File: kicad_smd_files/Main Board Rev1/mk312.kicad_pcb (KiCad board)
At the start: 4 copper layers, 135 x 83.5 mm, 171 parts, among them IC1 LD1086BDTTR, IC2 L7805CV, IC3 L7809ABV, IC4 L7809ABV, J1 Barrel_Jack_MountingPin, J10 OUTPUT B, J11 Conn_01x24_Male, J12 Conn_01x24_Male, J2 +12V Battery, J3 Conn_02x03_Odd_Even, J4 RADIO INTERFACE, J5 MIC INPUT, J6 LINE INPUT, J7 REMOTE INPUT, J8 LINK INPUT, J9 OUTPUT A, Q1 MMBT3904-7-F, Q2 MMBT3904-7-F, Q3 DMN10H170SK3-13, Q4 DMP6180SK3-13, Q5 DMN10H170SK3-13, Q6 DMN10H170SK3-13, Q7 DMP6180SK3-13, Q8 DMN10H170SK3-13, SW2 LEFT/DOWN, SW3 OK, SW4 RIGHT/UP, SW5 MENU, U1 ATmega16-16AU, U2 MCP6L01U, U3 CD4006B, U4 SP232E, U6 LM324N, U7 LM358N, U8 LTC1661

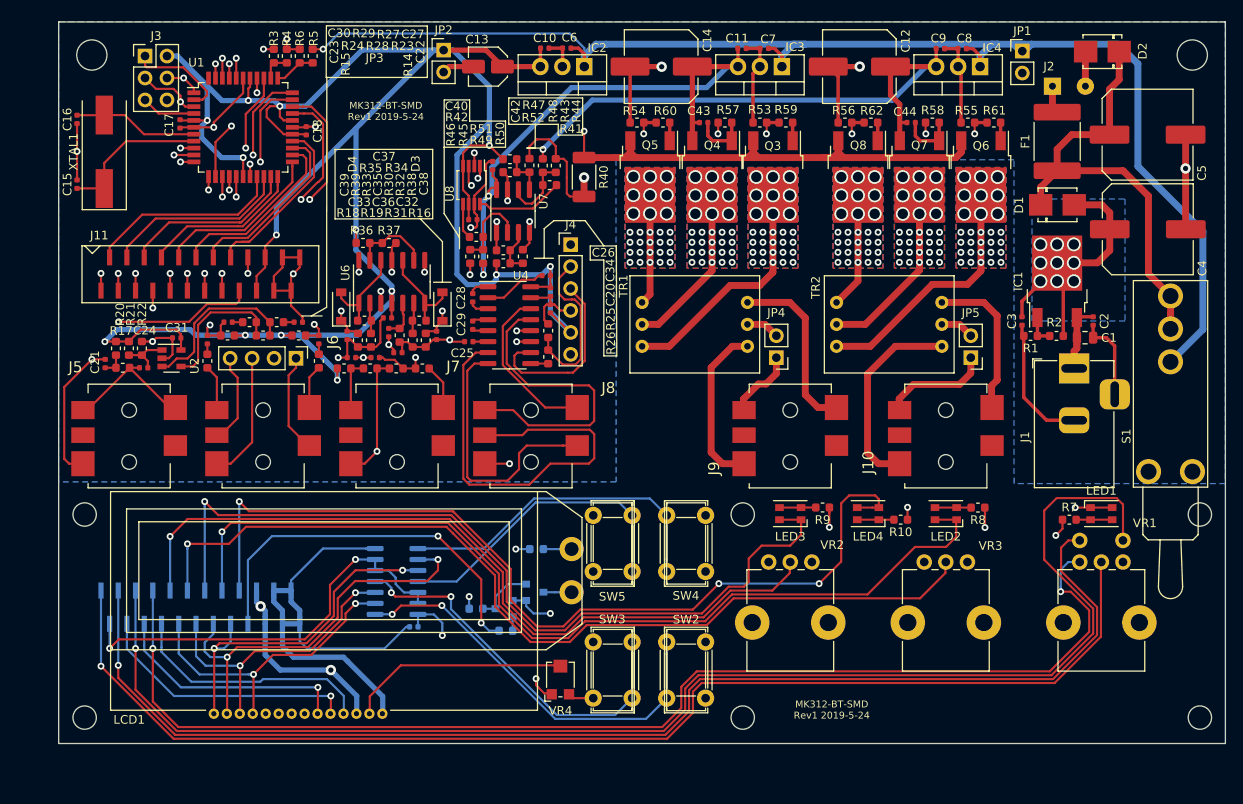
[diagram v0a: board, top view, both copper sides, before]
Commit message: Smaller PCB, cheaper parts
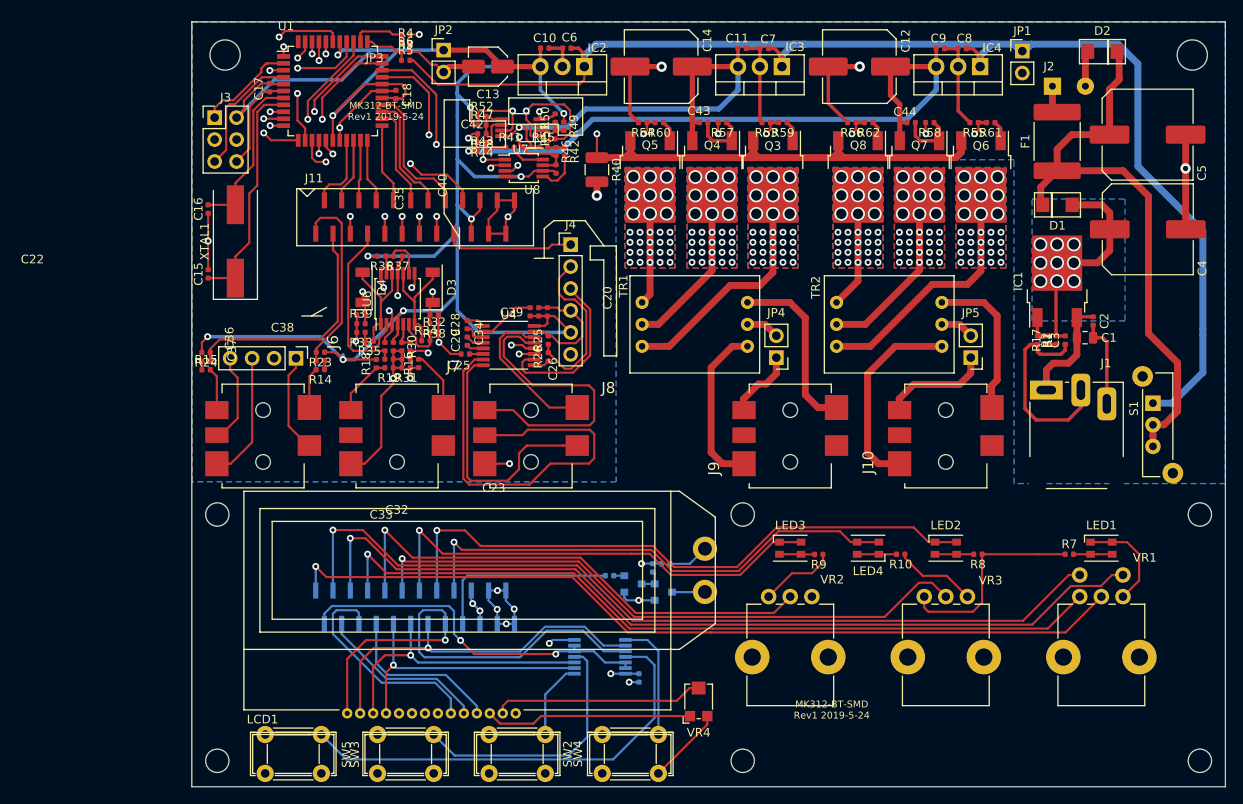
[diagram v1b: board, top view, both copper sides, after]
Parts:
- removed C21, C27, C30: 1uF, Capacitor_SMD:C_0402_1005Metric
- removed C24, C31: 0.1uF, Capacitor_SMD:C_0402_1005Metric
- removed J5: MIC INPUT, mk312-smd-footprints:SJ13515SMTTR
- removed R20: 2.2K, Resistor_SMD:R_0603_1608Metric
- removed R21, R22: 100K, Resistor_SMD:R_0603_1608Metric
- removed R27: 20K, Resistor_SMD:R_0603_1608Metric
- removed R28: 1M, Resistor_SMD:R_0603_1608Metric
- removed R29: 4.7K, Resistor_SMD:R_0603_1608Metric
- removed U2: MCP6L01U, Package_TO_SOT_SMD:SOT-23-5
- C13: footprint Capacitor_SMD:C_Elec_4x5.8 -> Capacitor_SMD:C_Elec_4x5.4
- D1, D2: value GF1G-E3/67A -> 583-FM4004W-W; footprint mk312-smd-footprints:DO-214BA -> mk312-smd-footprints:DO-214AC
- D3, D4: value 1N4148W-E3-08 -> LL4148; footprint Diode_SMD:D_SOD-123 -> mk312-smd-footprints:LL4148_SOD_80
- J1: footprint Connector_BarrelJack:BarrelJack_Horizontal -> mk312-smd-footprints:DJ_Jack_PJ-003A
- Q1, Q2: value MMBT3904-7-F -> MMBT3904
- Q3, Q5, Q6, Q8: value DMN10H170SK3-13 -> FQD13N10LTM
- Q4, Q7: value DMP6180SK3-13 -> FQD17P06TM
- R1: value 1K -> 100K; footprint Resistor_SMD:R_0603_1608Metric -> Resistor_SMD:R_0402_1005Metric
- R10, R11, R12, R13, R14, R15, R16, R18, R19, R23, R24, R25, R26, R30, R31, R38, R39, R5, R53, R54, R55, R56, R57, R58, R59, R6, R60, R61, R62, R7, R8, R9: footprint Resistor_SMD:R_0603_1608Metric -> Resistor_SMD:R_0402_1005Metric
- R17: value 2.2K -> 1K; footprint Resistor_SMD:R_0603_1608Metric -> Resistor_SMD:R_0402_1005Metric
- R2: value 110 -> 10K; footprint Resistor_SMD:R_0603_1608Metric -> Resistor_SMD:R_0402_1005Metric
- R3, R41, R42, R43, R44, R45, R46, R47, R49, R51, R52: value 100K -> 10K; footprint Resistor_SMD:R_0603_1608Metric -> Resistor_SMD:R_0402_1005Metric
- R32, R33, R4: value 20K -> 2K; footprint Resistor_SMD:R_0603_1608Metric -> Resistor_SMD:R_0402_1005Metric
- R34, R35: value 1M -> 100K; footprint Resistor_SMD:R_0603_1608Metric -> Resistor_SMD:R_0402_1005Metric
- R36: value 1M -> 20K; footprint Resistor_SMD:R_0603_1608Metric -> Resistor_SMD:R_0402_1005Metric
- R37: value 100K -> 2K; footprint Resistor_SMD:R_0603_1608Metric -> Resistor_SMD:R_0402_1005Metric
- R40: footprint Resistor_SMD:R_2010_5025Metric -> Resistor_SMD:R_1210_3225Metric
- R48, R50: value 200K -> 20K; footprint Resistor_SMD:R_0603_1608Metric -> Resistor_SMD:R_0402_1005Metric
- S1: footprint mk312-smd-footprints:E-Switch_M7_SPDT -> mk312-smd-footprints:SW_E-Switch-LC-1258
- U3: value CD4006B -> CD4066B; footprint Package_SO:SOIC-14_3.9x8.7mm_P1.27mm -> Package_SO:TSSOP-14_4.4x5mm_P0.65mm
- U4: value SP232E -> MAX202; footprint Package_SO:SOIC-16_3.9x9.9mm_P1.27mm -> Package_SO:TSSOP-16_4.4x5mm_P0.65mm
- U6: footprint Package_SO:SOIC-14_3.9x8.7mm_P1.27mm -> Package_SO:TSSOP-14_4.4x5mm_P0.65mm
- U7: footprint Package_SO:SOIC-8_3.9x4.9mm_P1.27mm -> Package_SO:VSSOP-8_3.0x3.0mm_P0.65mm
- moved R17 107.0 mm to (189.9, 59.3), turned to 90 degrees
- moved SW5 44.3 mm to (102.7, 107.2), turned to 270 degrees
- moved C19 26.7 mm to (142.7, 98.4), turned to 270 degrees
- moved SW3 25.9 mm to (115.7, 107.2), turned to 270 degrees
- moved J11 25.7 mm to (105.3, 47.0)
- moved SW4 25.2 mm to (141.7, 107.2), turned to 270 degrees
- moved U3 25.1 mm to (138.2, 96.0)
- moved J12 24.9 mm to (105.3, 88.3)
- moved SW2 21.8 mm to (128.7, 107.2), turned to 270 degrees
- moved R13 21.0 mm to (144.3, 85.7), turned to 90 degrees
- moved C15 18.4 mm to (92.9, 51.7)
- moved C16 18.4 mm to (92.9, 44.2)
- moved XTAL1 18.4 mm to (96.0, 47.9)
- moved R49 17.3 mm to (134.1, 34.6), turned to 270 degrees
- moved R50 16.4 mm to (133.1, 33.6)
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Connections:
- R17 pad 1: Net-(C21-Pad1) -> Net-(R17-Pad1)
- R17 pad 2: Net-(C24-Pad1) -> Net-(IC1-Pad1)
- R2 pad 1: Net-(IC1-Pad1) -> Net-(R17-Pad1)
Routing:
- net STATE: track 82.3 -> 15.1 mm, vias 1 -> 0
- net PA1-PANEL: track 161.1 -> 102.0 mm
- net RB4-PANEL: track 140.2 -> 91.7 mm, vias 2 -> 1
- net STATE-PANEL: track 106.3 -> 58.6 mm, vias 3 -> 1
- net +5V: track 282.0 -> 234.9 mm, vias 14 -> 10
- net RB9-PANEL: track 146.6 -> 100.0 mm
- net RB10-PANEL: track 142.9 -> 98.6 mm
- net PD6-PANEL: track 98.0 -> 54.8 mm
- net PD5-PANEL: track 109.2 -> 71.5 mm
- net +5VD: track 186.8 -> 152.0 mm, vias 9 -> 4
- net PA5-PANEL: track 106.1 -> 71.7 mm
- net PA4-PANEL: track 90.6 -> 58.7 mm
- net Net-(SW2-Pad1): track 47.1 -> 15.5 mm, vias 2 -> 0
- net PD2: track 34.0 -> 60.9 mm
- net PA1: track 85.6 -> 61.5 mm
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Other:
- board size 135 x 83.5 mm -> 119.6 x 88.5 mm

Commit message: part footprint corrections
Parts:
- C12, C14: footprint Capacitor_SMD:C_Elec_8x10.2 -> Capacitor_SMD:CP_Elec_8x10
- C13: footprint Capacitor_SMD:C_Elec_4x5.4 -> Capacitor_SMD:CP_Elec_4x5.4
- C4, C5: footprint Capacitor_SMD:C_Elec_10x10.2 -> Capacitor_SMD:CP_Elec_10x10
- moved S1 2.19 mm to (204.4, 66.4)
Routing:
- net +12V: track 157.8 -> 156.5 mm
